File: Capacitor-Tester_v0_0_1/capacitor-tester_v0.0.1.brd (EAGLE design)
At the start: 100 x 80 mm, 15 parts, among them IC1 AD8531ARZ, J1 USB4125-GF-A-0190_REVA2, U1 AD5933, Y1 LFSPXO018034

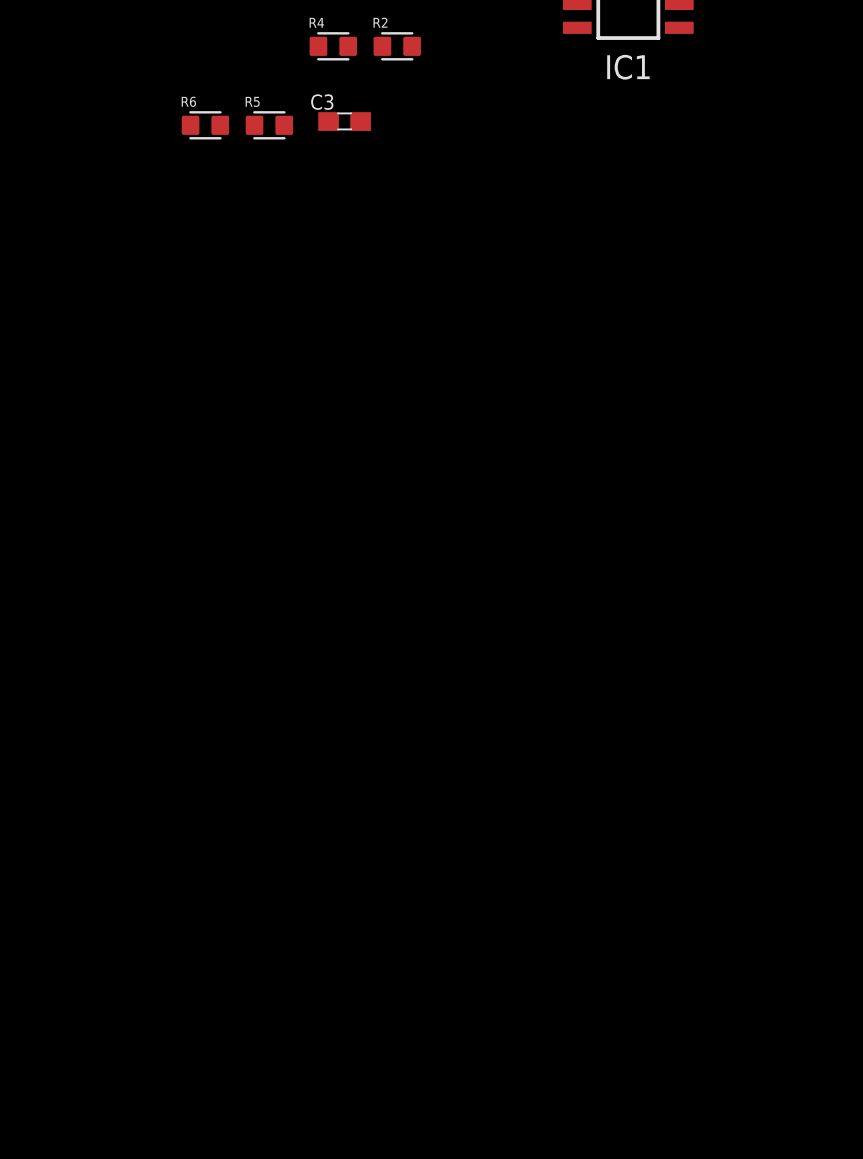
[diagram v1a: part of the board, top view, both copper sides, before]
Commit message: v0.0.1 - Added two stages of the opamps. Need to add boost converter for the second opamp
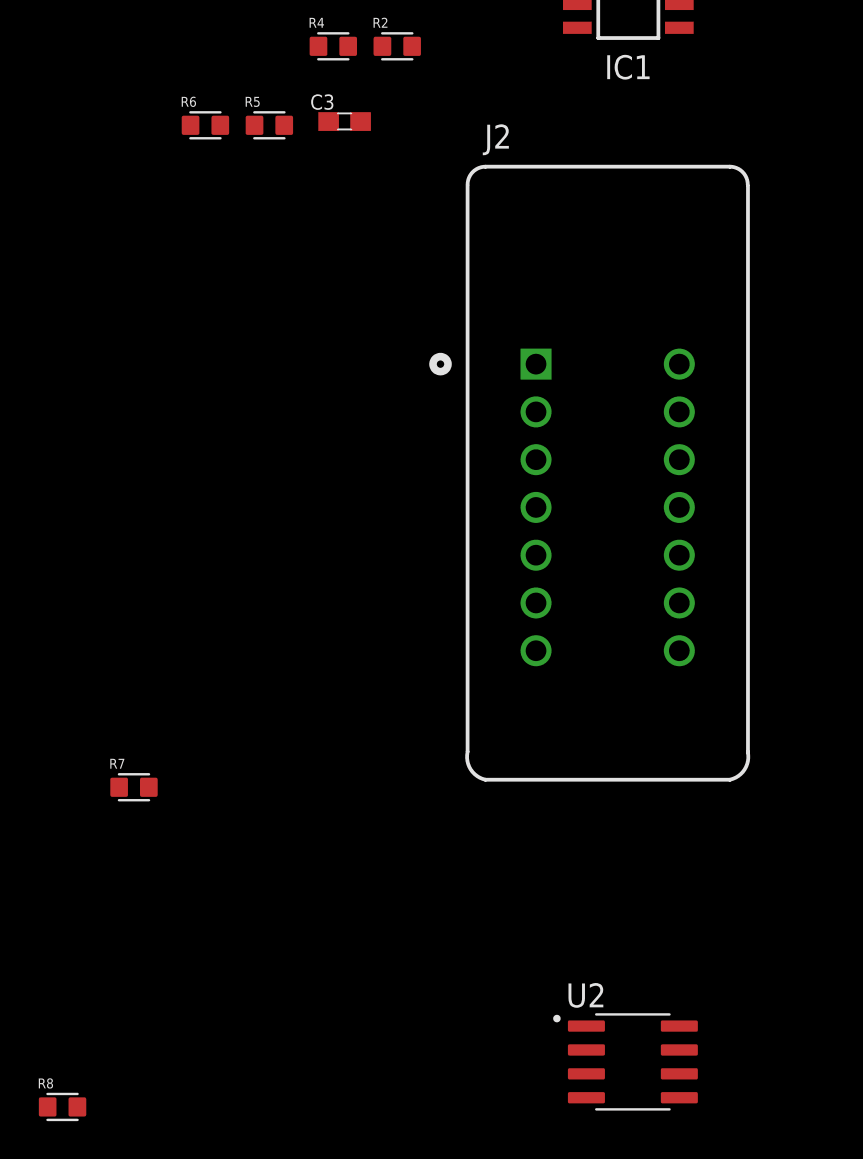
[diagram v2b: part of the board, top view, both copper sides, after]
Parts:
- added J2: DS1044-140G, DS1044-140G:CONNFLY_DS1044-140G
- added R7: DNP-100R-1%, custom_library:R0603
- added R8: 10k-1%, custom_library:R0603
- added U2: LM6171AIMX/NOPB, LM6171AIMX_NOPB:SOIC127P599X175-8N
- R1, R3: value DNP4k7-1% -> DNP-4k7-1%
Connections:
- new net N$2: R8.2, U2.2
- new net N$3: R8.1, U2.6
- new net VOUT_2: J2.10, J2.11, J2.12, J2.13, J2.14, J2.8, J2.9, R7.1
- net +5V: now also U2.7
- net GND: now also U2.3, U2.4
- net OPAMP_OUT: now also J2.1, J2.2, J2.3, J2.4, J2.5, J2.6, J2.7
- net RFB: now also R7.2
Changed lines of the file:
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@@
 <attribute name="SNAPEDA_LINK" value="https://www.snapeda.com/parts/USB4125-GF-A-0190/Global+Connector+Technology/view-part/?ref=snap" x="-4.6" y="-81.4" size="1.778" layer="27" display="off"/>
 </element>
-<element name="R3" library="custom_library" package="R0603" value="DNP4k7-1%" x="-7.2" y="-86.8" smashed="yes">
+<element name="R3" library="custom_library" package="R0603" value="DNP-4k7-1%" x="-7.2" y="-86.8" smashed="yes">
 <attribute name="NAME" x="-8.52476875" y="-85.813721875" size="0.52744375" layer="25"/>
 <attribute name="VALUE" x="-8.919259375" y="-88.32958125" size="0.525771875" layer="27"/>
 </element>
-<element name="R1" library="custom_library" package="R0603" value="DNP4k7-1%" x="-11.2" y="-86.8" smashed="yes">
+<element name="R1" library="custom_library" package="R0603" value="DNP-4k7-1%" x="-11.2" y="-86.8" smashed="yes">
 <attribute name="NAME" x="-12.52476875" y="-85.813721875" size="0.52744375" layer="25"/>
 <attribute name="VALUE" x="-12.919259375" y="-88.32958125" size="0.525771875" layer="27"/>
@@
 <attribute name="NAME" x="-26.52476875" y="-114.413721875" size="0.52744375" layer="25"/>
 <attribute name="VALUE" x="-26.919259375" y="-116.92958125" size="0.525771875" layer="27"/>
+</element>
+<element name="J2" library="DS1044-140G" package="CONNFLY_DS1044-140G" value="DS1044-140G" x="-3.81" y="-135.72" smashed="yes">
+<attribute name="AVAILABILITY" value="Not in stock" x="-3.81" y="-135.72" size="1.778" layer="27" display="off"/>
+<attribute name="CHECK_PRICES" value="https://www.snapeda.com/parts/DS1044-140G/Connfly/view-part/?ref=eda" x="-3.81" y="-135.72" size="1.778" layer="27" display="off"/>
+<attribute name="DESCRIPTION" value="                                                      Socket: DIP; ZIF; PIN: 14; 7.62mm; demountable; -40÷105°C; THT; 50VDC                                              " x="-3.81" y="-135.72" size="1.778" layer="27" display="off"/>
+<attribute name="MF" value="Connfly" x="-3.81" y="-135.72" size="1.778" layer="27" display="off"/>
+<attribute name="MP" value="DS1044-140G" x="-3.81" y="-135.72" size="1.778" layer="27" display="off"/>
+<attribute name="NAME" x="-10.369790625" y="-116.6415" size="1.2719" layer="25"/>
+<attribute name="PACKAGE" value="None" x="-3.81" y="-135.72" size="1.778" layer="27" display="off"/>
+<attribute name="PRICE" value="None" x="-3.81" y="-135.72" size="1.778" layer="27" display="off"/>
+<attribute name="SNAPEDA_LINK" value="https://www.snapeda.com/parts/DS1044-140G/Connfly/view-part/?ref=snap" x="-3.81" y="-135.72" size="1.778" layer="27" display="off"/>
+<attribute name="VALUE" x="-10.514840625" y="-152.1319" size="1.27091875" layer="27"/>
+</element>
+<element name="R7" library="custom_library" package="R0603" value="DNP-100R-1%" x="-29" y="-150.6" smashed="yes">
+<attribute name="NAME" x="-30.32476875" y="-149.613721875" size="0.52744375" layer="25"/>
+<attribute name="VALUE" x="-30.719259375" y="-152.12958125" size="0.525771875" layer="27"/>
+</element>
+<element name="U2" library="LM6171AIMX_NOPB" package="SOIC127P599X175-8N" value="LM6171AIMX/NOPB" x="-2.47" y="-165.205" smashed="yes">
+<attribute name="AVAILABILITY" value="In Stock" x="-2.47" y="-165.205" size="1.778" layer="27" display="off"/>
+<attribute name="CHECK_PRICES" value="https://www.snapeda.com/parts/LM6171AIMX/NOPB/Texas+Instruments/view-part/?ref=eda" x="-2.47" y="-165.205" size="1.778" layer="27" display="off"/>
+<attribute name="DESCRIPTION" value="                                                      High Speed, Low Power, Low Distortion Voltage Feedback Amplifier                                              " x="-2.47" y="-165.205" size="1.778" layer="27" display="off"/>
+<attribute name="MF" value="Texas Instruments" x="-2.47" y="-165.205" size="1.778" layer="27" display="off"/>
+<attribute name="MP" value="LM6171AIMX/NOPB" x="-2.47" y="-165.205" size="1.778" layer="27" display="off"/>
+<attribute name="NAME" x="-6.03" y="-162.303" size="1.27" layer="25"/>
+<attribute name="PACKAGE" value="SOIC-8 Texas Instruments" x="-2.47" y="-165.205" size="1.778" layer="27" display="off"/>
+<attribute name="PRICE" value="None" x="-2.47" y="-165.205" size="1.778" layer="27" display="off"/>
+<attribute name="SNAPEDA_LINK" value="https://www.snapeda.com/parts/LM6171AIMX/NOPB/Texas+Instruments/view-part/?ref=snap" x="-2.47" y="-165.205" size="1.778" layer="27" display="off"/>
+<attribute name="VALUE" x="-6.03" y="-168.107" size="1.27" layer="27" align="top-left"/>
+</element>
+<element name="R8" library="custom_library" package="R0603" value="10k-1%" x="-32.8" y="-167.6" smashed="yes">
+<attribute name="NAME" x="-34.12476875" y="-166.613721875" size="0.52744375" layer="25"/>
+<attribute name="VALUE" x="-34.519259375" y="-169.12958125" size="0.525771875" layer="27"/>
 </element>
 </elements>
@@
 <contactref element="C3" pad="2"/>
 <contactref element="R6" pad="2"/>
-<wire x1="-16.95" y1="-115.2" x2="-24.41" y2="-115.4" width="0" layer="19" extent="1-1"/>
+<contactref element="U2" pad="4"/>
+<contactref element="U2" pad="3"/>
+<wire x1="-4.94" y1="-165.84" x2="-4.94" y2="-167.11" width="0" layer="19" extent="1-1"/>
+<wire x1="-16.95" y1="-115.2" x2="-4.94" y2="-165.84" width="0" layer="19" extent="1-1"/>
+<wire x1="-24.41" y1="-115.4" x2="-16.95" y2="-115.2" width="0" layer="19" extent="1-1"/>
 <wire x1="-5.424" y1="-110.215" x2="-16.95" y2="-115.2" width="0" layer="19" extent="1-1"/>
 <wire x1="-8.92" y1="-82.2" x2="-5.424" y2="-110.215" width="0" layer="19" extent="1-1"/>
@@
 <contactref element="IC1" pad="7"/>
 <contactref element="R5" pad="1"/>
+<contactref element="U2" pad="7"/>
+<wire x1="-22.59" y1="-115.4" x2="0" y2="-164.57" width="0" layer="19" extent="1-1"/>
 <wire x1="0" y1="-107.675" x2="-22.59" y2="-115.4" width="0" layer="19" extent="1-1"/>
 <wire x1="-6.41" y1="-86.8" x2="0" y2="-107.675" width="0" layer="19" extent="1-1"/>
@@
 <signal name="RFB">
 <contactref element="U1" pad="4"/>
+<contactref element="R7" pad="2"/>
+<wire x1="-7.01" y1="-14.65" x2="-28.21" y2="-150.6" width="0" layer="19" extent="1-1"/>
 </signal>
 <signal name="VIN">
@@
 <contactref element="IC1" pad="6"/>
 <contactref element="R4" pad="2"/>
+<contactref element="J2" pad="1"/>
+<contactref element="J2" pad="7"/>
+<contactref element="J2" pad="6"/>
+<contactref element="J2" pad="5"/>
+<contactref element="J2" pad="4"/>
+<contactref element="J2" pad="3"/>
+<contactref element="J2" pad="2"/>
+<wire x1="-7.62" y1="-140.8" x2="-7.62" y2="-143.34" width="0" layer="19" extent="1-1"/>
+<wire x1="-7.62" y1="-138.26" x2="-7.62" y2="-140.8" width="0" layer="19" extent="1-1"/>
+<wire x1="-7.62" y1="-135.72" x2="-7.62" y2="-138.26" width="0" layer="19" extent="1-1"/>
+<wire x1="-7.62" y1="-133.18" x2="-7.62" y2="-135.72" width="0" layer="19" extent="1-1"/>
+<wire x1="-7.62" y1="-130.64" x2="-7.62" y2="-133.18" width="0" layer="19" extent="1-1"/>
+<wire x1="-7.62" y1="-128.1" x2="-7.62" y2="-130.64" width="0" layer="19" extent="1-1"/>
+<wire x1="-17.61" y1="-111.2" x2="-7.62" y2="-128.1" width="0" layer="19" extent="1-1"/>
 <wire x1="0" y1="-108.945" x2="-17.61" y2="-111.2" width="0" layer="19" extent="1-1"/>
 </signal>
@@
 <wire x1="-5.424" y1="-108.945" x2="-18.65" y2="-115.2" width="0" layer="19" extent="1-1"/>
 </signal>
+<signal name="VOUT_2">
+<contactref element="J2" pad="14"/>
+<contactref element="J2" pad="13"/>
+<contactref element="J2" pad="12"/>
+<contactref element="J2" pad="8"/>
+<contactref element="J2" pad="11"/>
+<contactref element="J2" pad="10"/>
+<contactref element="J2" pad="9"/>
+<contactref element="R7" pad="1"/>
+<wire x1="0" y1="-143.34" x2="-29.79" y2="-150.6" width="0" layer="19" extent="1-1"/>
+<wire x1="0" y1="-140.8" x2="0" y2="-143.34" width="0" layer="19" extent="1-1"/>
+<wire x1="0" y1="-138.26" x2="0" y2="-140.8" width="0" layer="19" extent="1-1"/>
+<wire x1="0" y1="-135.72" x2="0" y2="-138.26" width="0" layer="19" extent="1-1"/>
+<wire x1="0" y1="-133.18" x2="0" y2="-135.72" width="0" layer="19" extent="1-1"/>
+<wire x1="0" y1="-130.64" x2="0" y2="-133.18" width="0" layer="19" extent="1-1"/>
+<wire x1="0" y1="-128.1" x2="0" y2="-130.64" width="0" layer="19" extent="1-1"/>
+</signal>
+<signal name="N$2">
+<contactref element="U2" pad="2"/>
+<contactref element="R8" pad="2"/>
+<wire x1="-4.94" y1="-164.57" x2="-32.01" y2="-167.6" width="0" layer="19" extent="1-1"/>
+</signal>
+<signal name="N$3">
+<contactref element="R8" pad="1"/>
+<contactref element="U2" pad="6"/>
+<wire x1="0" y1="-165.84" x2="-33.59" y2="-167.6" width="0" layer="19" extent="1-1"/>
+</signal>
 </signals>

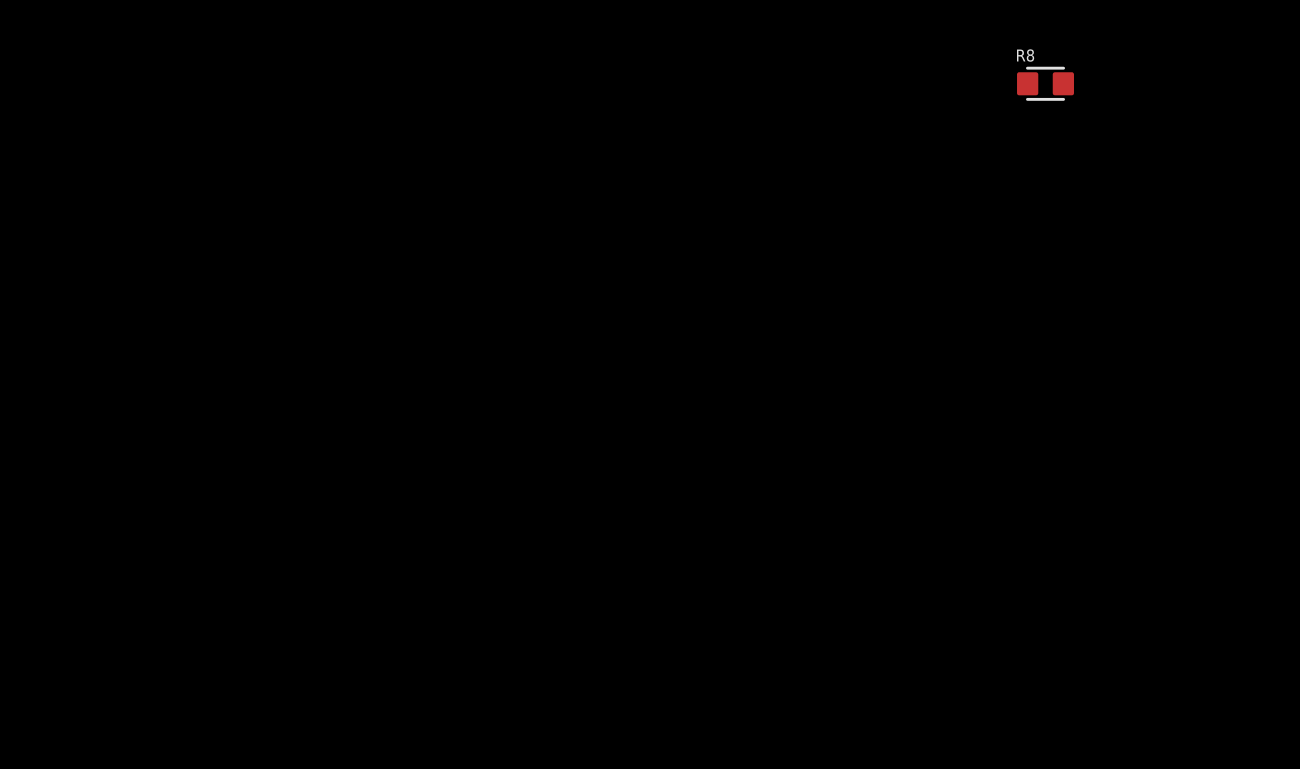
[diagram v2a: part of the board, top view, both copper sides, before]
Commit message: v0.0.1 - Added 5V -> 15V boost converter for the second stage opamp.
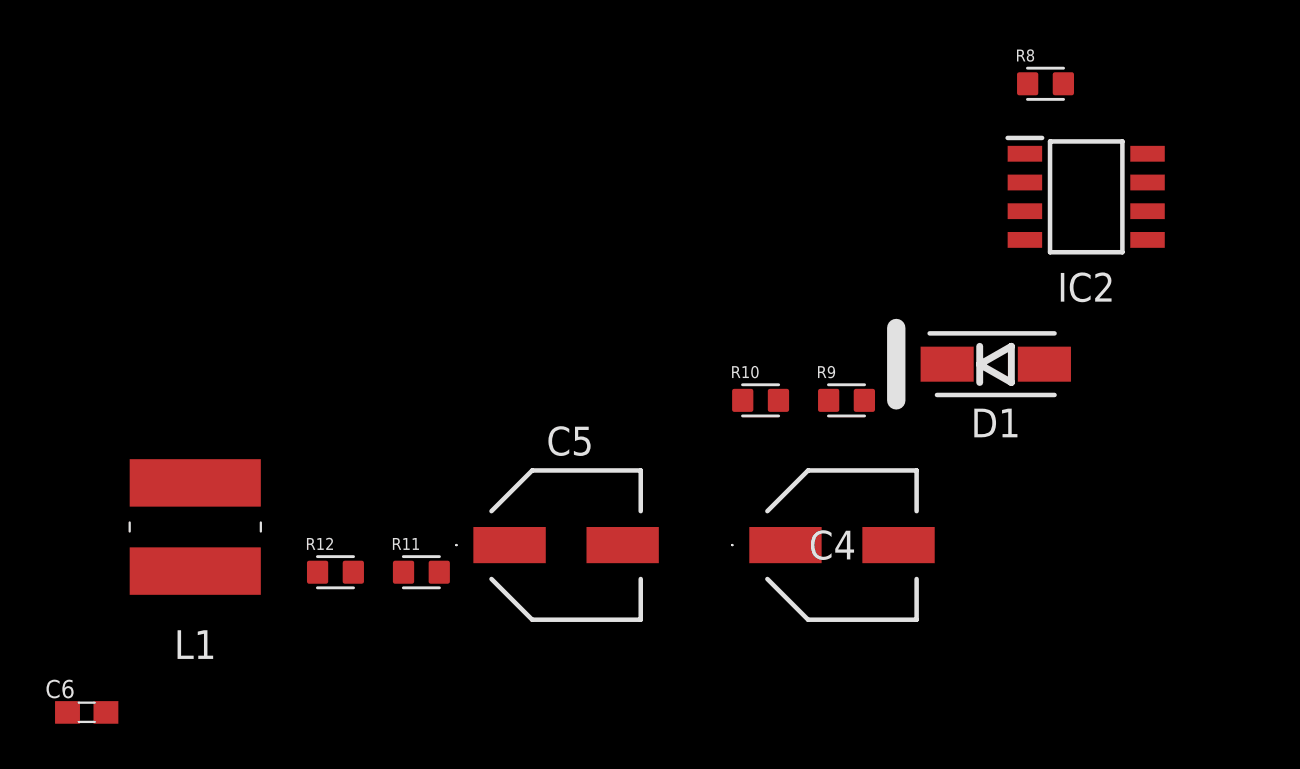
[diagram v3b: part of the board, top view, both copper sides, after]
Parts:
- added C4: EEEFKC271XSP, EEEFKC271XSP:EEE0JA331XP
- added C5: VS1C101ME054000CE0, EEEFKC271XSP:EEE0JA331XP
- added C6: 560p, custom_library:C0603
- added D1: SS14, SS14:DIOM5227X270N
- added IC2: MC34063EBD-TR, MC34063EBD-TR:SOIC127P600X175-8N
- added L1: SDR0604-221KL, SDR0604-221KL:SDR0604221KL
- added R10: 910R-1%, custom_library:R0603
- added R11: 0603WAJ022KT5E, custom_library:R0603
- added R12: 180R-1%, custom_library:R0603
- added R9: 10k-1%, custom_library:R0603
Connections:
- new net +15V: C4.1, D1.1, R9.1, U2.7
- new net N$10: C6.1, IC2.3
- new net N$11: IC2.7, L1.1, R11.2, R12.2
- new net N$5: D1.2, IC2.1, L1.2
- new net N$7: IC2.5, R10.1, R9.2
- new net N$8: IC2.8, R12.1
- net +5V: now also C5.1, IC2.6, R11.1; no longer U2.7
- net GND: now also C4.2, C5.2, C6.2, IC2.2, IC2.4, R10.2

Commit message: v0.0.1 - Added input connector
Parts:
- added J3: 250-102, custom_library:CONN_250-102_WAG
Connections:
- net SCL: now also J3.2
- net SDA: now also J3.1
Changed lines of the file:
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@@
 <attribute name="VALUE" x="-75.835" y="-197.305" size="1.27" layer="27"/>
+</element>
+<element name="J3" library="custom_library" package="CONN_250-102_WAG" value="250-102" x="-90.8" y="-175.2" smashed="yes">
+<attribute name="COPYRIGHT" value="Copyright (C) 2024 Ultra Librarian. All rights reserved." x="-90.8" y="-175.2" size="1.778" layer="27" display="off"/>
+<attribute name="MANUFACTURER_PART_NUMBER" value="250-102" x="-90.8" y="-175.2" size="1.778" layer="27" display="off"/>
+<attribute name="MFR_NAME" value="Wago" x="-90.8" y="-175.2" size="1.778" layer="27" display="off"/>
+<attribute name="NAME" x="-93.0606" y="-175.835" size="1.27" layer="27" ratio="6" rot="SR0"/>
+<attribute name="VALUE" x="-91.5366" y="-175.835" size="1.27" layer="27" ratio="6" rot="SR0"/>
 </element>
 </elements>
@@
 <contactref element="U1" pad="16"/>
 <contactref element="R1" pad="1"/>
+<contactref element="J3" pad="2"/>
 <wire x1="0" y1="-12.7" x2="-11.99" y2="-86.8" width="0" layer="19" extent="1-1"/>
+<wire x1="-87.2948" y1="-175.2" x2="-11.99" y2="-86.8" width="0" layer="19" extent="1-1"/>
 </signal>
 <signal name="SDA">
 <contactref element="U1" pad="15"/>
 <contactref element="R3" pad="1"/>
+<contactref element="J3" pad="1"/>
 <wire x1="0" y1="-13.35" x2="-7.99" y2="-86.8" width="0" layer="19" extent="1-1"/>
+<wire x1="-90.8" y1="-175.2" x2="-7.99" y2="-86.8" width="0" layer="19" extent="1-1"/>
 </signal>
 <signal name="MCLK">
